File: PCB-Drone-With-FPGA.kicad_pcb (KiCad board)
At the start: 4 copper layers, 100 x 100 mm, 45 parts, among them J501 SMA-RP, U1 10CL040_F484, U401 ICM-20948, U402 BNO055, U403 DPS422XTSA1, U404 MCP3208, U405 TXB0104PWR, U501 nRF24L01P, U502 RFX2401C, X501 16MHz

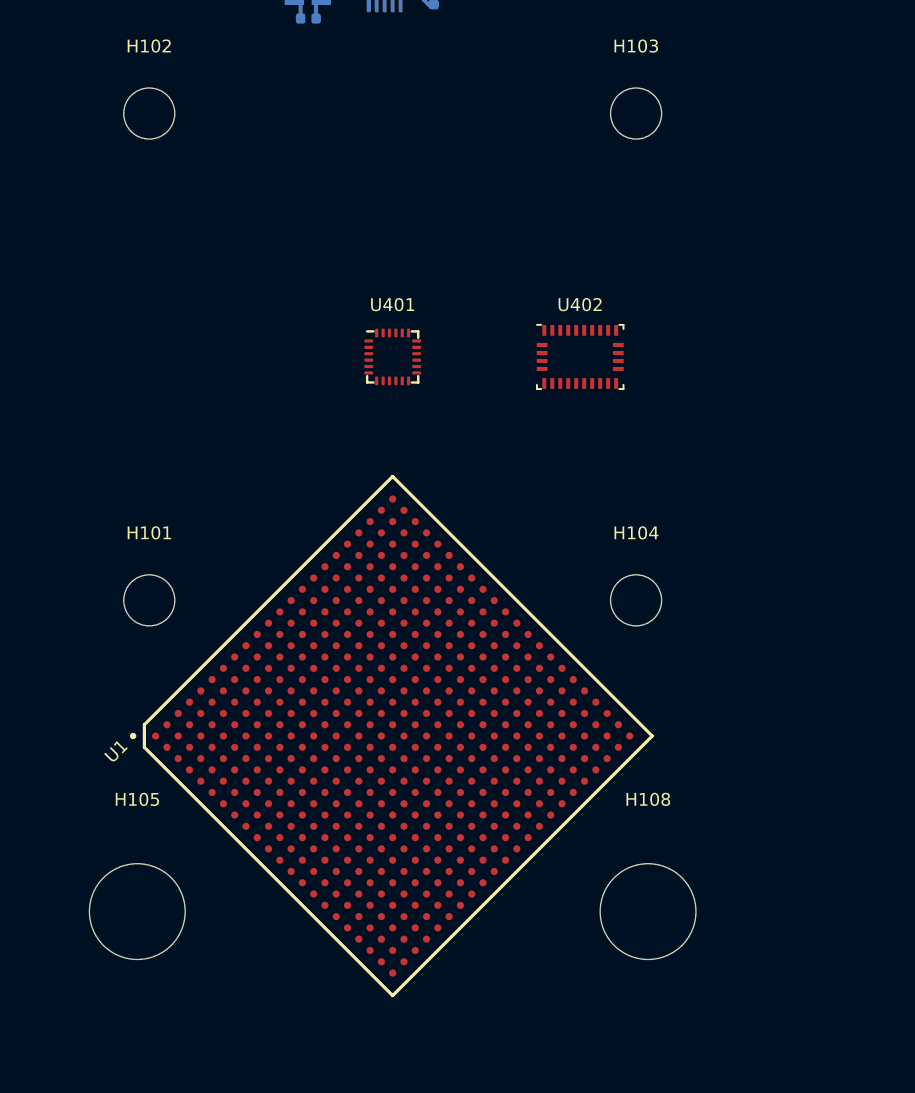
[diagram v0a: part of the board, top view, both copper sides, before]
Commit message: Continued work on schematic and board planning
Signed-off-by: Eldalote <Eldalote.Electronics@gmail.com>
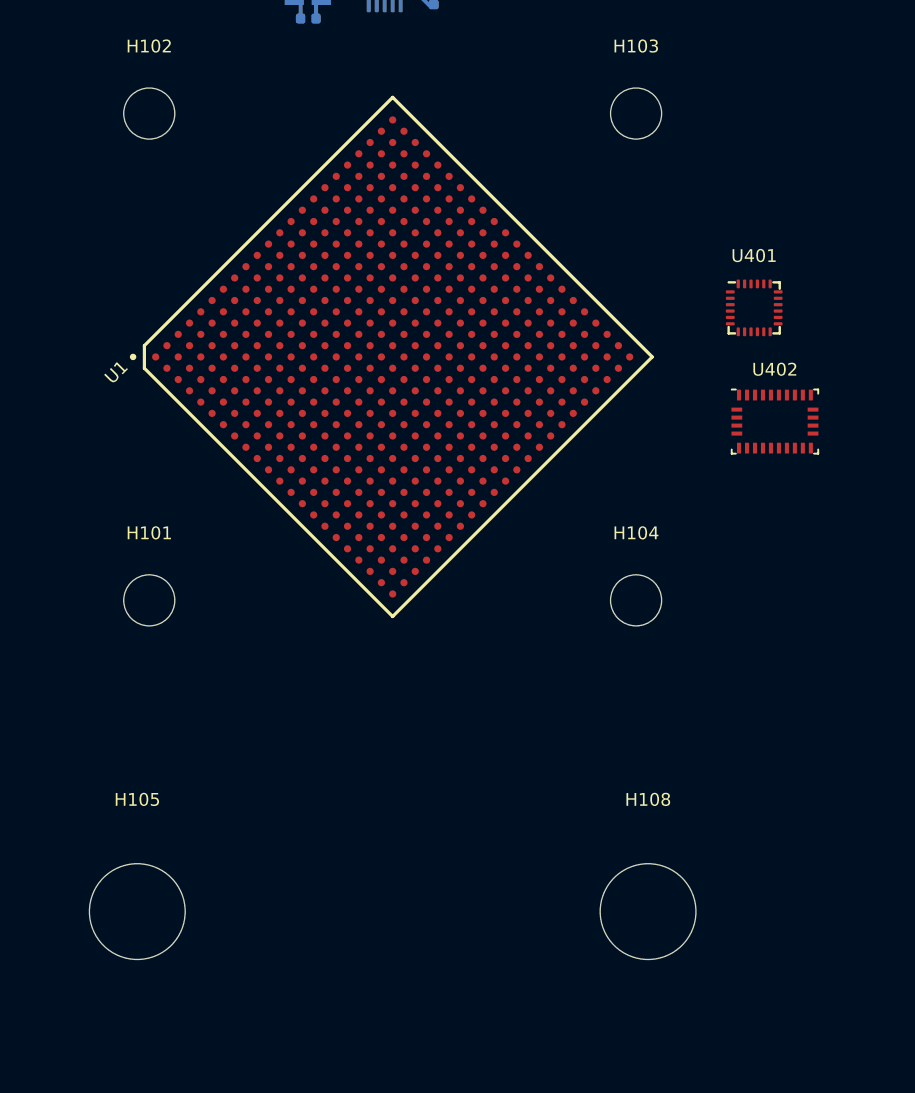
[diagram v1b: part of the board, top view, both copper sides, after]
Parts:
- moved U1 23.8 mm to (150.2, 100.2)
- moved U401 22.9 mm to (172.9, 97.2)
- moved U402 12.9 mm to (174.2, 104.3)

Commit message: More of the same
Signed-off-by: Eldalote <Eldalote.Electronics@gmail.com>
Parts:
- removed H107, H108: MountingHole, MountingHole:MountingHole_6mm
- added J201: PJ-102A, digikey-footprints:Barrel_Jack_5.5mmODx2.1mmID_PJ-102A, F.Cu at (152.5, 134.9)
- added J601: Conn_02x10_Row_Letter_First, Connector_PinHeader_2.54mm:PinHeader_2x10_P2.54mm_Vertical, F.Cu at (114.0, 42.7)
- added J602: Conn_02x10_Row_Letter_First, Connector_PinHeader_2.54mm:PinHeader_2x10_P2.54mm_Vertical, F.Cu at (144.0, 42.9)
- added JP201: Jumper_NC_Dual, Connector_PinHeader_2.54mm:PinHeader_1x03_P2.54mm_Vertical, F.Cu at (179.5, 122.1)
- added U201: TPS54331DR, SamacSys_Parts:SOIC127P600X175-8N, F.Cu at (112.7, 117.7)
- added U202: TPS54331DR, SamacSys_Parts:SOIC127P600X175-8N, F.Cu at (146.4, 108.9)
- added U203: TPS54331DR, SamacSys_Parts:SOIC127P600X175-8N, F.Cu at (153.5, 87.7)
- added U204: TPS73701DCQ, SamacSys_Parts:SOT127P706X180-6N, F.Cu at (106.3, 86.7)
- added U301: FT232H, Package_QFP:LQFP-48_7x7mm_P0.5mm, F.Cu at (130.3, 122.5)
- added U406: TXB0108PWR, digikey-footprints:TSSOP-20_W4.4mm, F.Cu at (120.9, 101.6)
- C501, C502, C503, C504, C505, C506, C507, C508, C509, C510, C511, C512, C513, C514, C515, C516, C517, J501, L501, L502, L503, L504, L505, R501, R502, R503, R504, U501, U502, X501: moved to F.Cu
- U1: moved to B.Cu
- U405: value TXB0104PWR -> TXB0108PWR; footprint digikey-footprints:TSSOP-14_W4.4mm -> digikey-footprints:TSSOP-20_W4.4mm
- moved U404 122.1 mm to (112.4, 107.5)
- moved U405 104.9 mm to (120.8, 109.0), turned to 90 degrees
- moved U403 98.3 mm to (138.2, 115.8)
- moved H105 63.3 mm to (114.8, 74.8)
- moved U401 44.8 mm to (130.0, 110.0)
- moved U402 37.0 mm to (137.6, 109.7)
- moved C512 29.7 mm to (126.1, 56.1)
- moved C503 29.2 mm to (126.4, 65.8)
- moved R501 28.3 mm to (126.9, 63.8), turned to 180 degrees
- moved C511 27.9 mm to (127.1, 55.1)
- moved C510 27.9 mm to (127.1, 57.1)
- moved C502 27.4 mm to (127.4, 65.8)
- moved C501 27.4 mm to (127.4, 67.7)
- moved U1 24.2 mm to (130.0, 87.0), turned to 315 degrees
- moved C513 24.1 mm to (129.1, 53.0), turned to 0 degrees
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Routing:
- net GND: track 18.1 -> 14.1 mm, vias 2 -> 0
- added copper zone on F.Cu, net GND
- removed copper zone on B.Cu, net GND
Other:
- board size 100 x 100 mm -> 60 x 100 mm

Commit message: Further work
Signed-off-by: Eldalote <Eldalote.Electronics@gmail.com>
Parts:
- removed J601, J602: Conn_02x10_Row_Letter_First, Connector_PinHeader_2.54mm:PinHeader_2x10_P2.54mm_Vertical
- added C201: 22uF 25v, Capacitor_SMD:C_0805_2012Metric, F.Cu at (86.5, 133.6)
- added C202: 10pF, Capacitor_SMD:C_0402_1005Metric, F.Cu at (80.1, 142.7)
- added C203: 1nF, Capacitor_SMD:C_0402_1005Metric, F.Cu at (85.8, 138.6)
- added C204: 8n2F, Capacitor_SMD:C_0603_1608Metric, F.Cu at (76.6, 142.9)
- added C205: 100nF, Capacitor_SMD:C_0402_1005Metric, F.Cu at (83.0, 142.7)
- added C206: 47uF, Resistor_SMD:R_1206_3216Metric, F.Cu at (66.2, 141.5)
- added C207: 47uF, Resistor_SMD:R_1206_3216Metric, F.Cu at (71.8, 143.3)
- added C208: 47uF, Resistor_SMD:R_1206_3216Metric, F.Cu at (66.2, 144.8)
- added D201: 3A 60v, Diode_SMD:D_SMC, F.Cu at (68.8, 136.0)
- added J301: UJ2-MBH-1-SMT-TR, digikey-footprints:USB_Mini_B_Female_UJ2-MBH-1-SMT-TR, F.Cu at (130.7, 139.7)
- added J701: Conn_02x10, Connector_PinHeader_2.54mm:PinHeader_2x10_P2.54mm_Vertical, F.Cu at (113.7, 42.9)
- added J702: Conn_02x07, Connector_PinHeader_2.54mm:PinHeader_2x07_P2.54mm_Vertical, F.Cu at (102.6, 103.1)
- added J703: Conn_02x10, Connector_PinHeader_2.54mm:PinHeader_2x10_P2.54mm_Vertical, F.Cu at (143.9, 43.2)
- added J704: Conn_02x04, Connector_PinHeader_2.54mm:PinHeader_2x04_P2.54mm_Vertical, F.Cu at (154.3, 116.8)
- added J705: Conn_02x05, Connector_PinHeader_2.54mm:PinHeader_2x05_P2.54mm_Vertical, F.Cu at (154.4, 93.8)
- added L201: 5u6H, Inductor_SMD:L_Bourns_SRN8040TA, F.Cu at (79.3, 136.9)
- added R201: 330K, Resistor_SMD:R_0402_1005Metric, F.Cu at (80.1, 144.7)
- added R202: 68K, Resistor_SMD:R_0402_1005Metric, F.Cu at (85.8, 140.6)
- added R203: 62K, Resistor_SMD:R_0603_1608Metric, F.Cu at (86.3, 136.3)
- added R204: 10K, Resistor_SMD:R_0402_1005Metric, F.Cu at (83.0, 144.7)
- added R205: 1.8K, Resistor_SMD:R_0603_1608Metric, F.Cu at (76.6, 145.4)
- added R206: 100R, Resistor_SMD:R_0402_1005Metric, F.Cu at (85.9, 142.6)
- moved JP201 75.4 mm to (104.2, 125.6)
- moved LOGO101 46.0 mm to (158.8, 73.8)
- moved U405 27.6 mm to (147.5, 116.0)
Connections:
- U201 pad 7: Net-(U201-Pad7) -> GND
- U202 pad 2: +10V -> Net-(U202-Pad2)
- U203 pad 2: +10V -> Net-(U203-Pad2)

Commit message: Made progress woth power
Signed-off-by: Jan Mart Liewes <Eldalote.Electronics@gmail.com>
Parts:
- removed C201: 22uF 25v, Capacitor_SMD:C_0805_2012Metric
- removed C202: 10pF, Capacitor_SMD:C_0402_1005Metric
- removed C203: 1nF, Capacitor_SMD:C_0402_1005Metric
- removed C204: 8n2F, Capacitor_SMD:C_0603_1608Metric
- removed C205: 100nF, Capacitor_SMD:C_0402_1005Metric
- removed C206, C207, C208: 47uF, Resistor_SMD:R_1206_3216Metric
- removed C505: 22pF, Capacitor_SMD:C_0402_1005Metric
- removed D201: 3A 60v, Diode_SMD:D_SMC
- removed L201: 5u6H, Inductor_SMD:L_Bourns_SRN8040TA
- removed R201: 330K, Resistor_SMD:R_0402_1005Metric
- removed R202: 68K, Resistor_SMD:R_0402_1005Metric
- removed R203: 62K, Resistor_SMD:R_0603_1608Metric
- removed R204: 10K, Resistor_SMD:R_0402_1005Metric
- removed R205: 1.8K, Resistor_SMD:R_0603_1608Metric
- removed R206: 100R, Resistor_SMD:R_0402_1005Metric
- removed U201, U202, U203: TPS54331DR, SamacSys_Parts:SOIC127P600X175-8N
- removed U204: TPS73701DCQ, SamacSys_Parts:SOT127P706X180-6N
- removed U405: TXB0108PWR, digikey-footprints:TSSOP-20_W4.4mm
- added C301: 10uF 25v, Capacitor_SMD:C_0805_2012Metric, F.Cu at (166.4, 56.2)
- added C302: 100nF 16v, Capacitor_SMD:C_0402_1005Metric, F.Cu at (170.1, 56.7)
- added C303: 22uF 25v, Capacitor_SMD:C_0805_2012Metric, F.Cu at (172.9, 54.2)
- added C304: 22uF 25v, Capacitor_SMD:C_0805_2012Metric, F.Cu at (178.1, 49.7)
- added C401: 10uF, Capacitor_SMD:C_0805_2012Metric, F.Cu at (191.6, 79.7)
- added C402: 1uF, Capacitor_SMD:C_0603_1608Metric, F.Cu at (196.1, 77.7)
- added C403: 1uF, Capacitor_SMD:C_0603_1608Metric, F.Cu at (195.8, 80.2)
- added C404: 22uF, Capacitor_SMD:C_0805_2012Metric, F.Cu at (196.2, 75.0)
- added C805: 15pF, Capacitor_SMD:C_0402_1005Metric, F.Cu at (135.2, 63.8)
- added L301: 4.7uH 2.6ADC, Eldalote-footprints:L_5030_TAIYO_YUDEN, F.Cu at (167.5, 51.5)
- added L401: 1uH, Eldalote-footprints:L_3012_TDK, F.Cu at (191.8, 75.7)
- added U301: AP63205WU-7, SamacSys_Parts:SOT95P280X100-6N, F.Cu at (173.3, 50.5)
- added U402: NCP115ASN250T2G, SamacSys_Parts:SOT95P275X110-5N, F.Cu at (186.9, 75.8)
- added U501: AP63200WU-7, SamacSys_Parts:SOT95P280X100-6N, F.Cu at (207.2, 75.8)
- C804: renamed from C504; value 22pF -> 15pF
- U401: value ICM-20948 -> SC189ZSKTRT; footprint Sensor_Motion:InvenSense_QFN-24_3x3mm_P0.4mm -> SamacSys_Parts:SOT95P280X145-5N
- moved U401 64.0 mm to (186.8, 80.5)
- renumbered C501 to C801, C502 to C802, C503 to C803, C506 to C806, C507 to C807, C508 to C808, C509 to C809, C510 to C810, C511 to C811, C512 to C812, C513 to C813, C514 to C814, C515 to C815, C516 to C816, C517 to C817, J701 to J1001, J702 to J1002, J703 to J1003, J704 to J1004, J705 to J1005, J301 to J601, J501 to J801, L501 to L801, L502 to L802, L503 to L803, L504 to L804, L505 to L805, R501 to R801, R502 to R802, R503 to R803, R504 to R804, U1 to U1201, U301 to U601, U402 to U701, U403 to U702, U404 to U703, U406 to U704, U501 to U801, U502 to U802, X501 to X801
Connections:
- U401 pad 1: Net-(U401-Pad1) -> +5V
- U401 pad 2: Net-(U401-Pad2) -> GND
- U401 pad 3: Net-(U401-Pad3) -> +5V
- U401 pad 4: Net-(U401-Pad4) -> +3V3

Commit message: Finished v0.1 of power, and v0.1 of sensors.
Signed-off-by: Jan Mart Liewes <Eldalote.Electronics@gmail.com>
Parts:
- added C501: 10uF, Capacitor_SMD:C_0805_2012Metric, F.Cu at (195.7, 97.6)
- added C502: 100nF, Capacitor_SMD:C_0402_1005Metric, F.Cu at (195.0, 100.1)
- added C503: 100pF, Capacitor_SMD:C_0402_1005Metric, F.Cu at (198.4, 103.0)
- added C504: 22uF, Capacitor_SMD:C_0805_2012Metric, F.Cu at (194.8, 103.3)
- added C505: 22uF, Capacitor_SMD:C_0805_2012Metric, F.Cu at (200.2, 97.6)
- added C701: 100nF, Capacitor_SMD:C_0402_1005Metric, F.Cu at (78.1, 100.1)
- added C702: 2u2F, Capacitor_SMD:C_0603_1608Metric, F.Cu at (74.6, 100.4)
- added C703: 100nF, Capacitor_SMD:C_0402_1005Metric, F.Cu at (78.8, 107.6)
- added C704: 10nF, Capacitor_SMD:C_0402_1005Metric, F.Cu at (74.1, 109.6)
- added C705: 100nF, Capacitor_SMD:C_0402_1005Metric, F.Cu at (75.9, 107.6)
- added C706: 100nF, Capacitor_SMD:C_0805_2012Metric_Pad1.15x1.40mm_HandSolder, F.Cu at (65.5, 100.6)
- added C707: 100nF, Capacitor_SMD:C_0805_2012Metric_Pad1.15x1.40mm_HandSolder, F.Cu at (60.4, 106.9)
- added C708: 100nF, Capacitor_SMD:C_0402_1005Metric, F.Cu at (73.6, 105.6)
- added C709: 100nF, Capacitor_SMD:C_0402_1005Metric, F.Cu at (78.1, 102.1)
- added C710: 4n7F, Capacitor_SMD:C_0603_1608Metric, F.Cu at (64.8, 109.6)
- added C711: 22pF, Capacitor_SMD:C_0603_1608Metric, F.Cu at (69.6, 107.9)
- added C712: 22pF, Capacitor_SMD:C_0603_1608Metric, F.Cu at (74.1, 103.3)
- added C713: 100nF, Capacitor_SMD:C_0402_1005Metric, F.Cu at (77.0, 109.6)
- added C714: 1uF, Capacitor_SMD:C_0805_2012Metric_Pad1.15x1.40mm_HandSolder, F.Cu at (65.2, 106.9)
- added C715: 100nF, Capacitor_SMD:C_0805_2012Metric_Pad1.15x1.40mm_HandSolder, F.Cu at (60.4, 109.9)
- added C716: 100nF, Capacitor_SMD:C_0402_1005Metric, F.Cu at (68.3, 110.1)
- added C717: 1uF, Capacitor_SMD:C_0805_2012Metric_Pad1.15x1.40mm_HandSolder, F.Cu at (70.2, 100.6)
- added C718: 100nF, Capacitor_SMD:C_0805_2012Metric_Pad1.15x1.40mm_HandSolder, F.Cu at (65.2, 104.0)
- added L501: 2u2H, Eldalote-footprints:L_4018_Bourns, F.Cu at (190.7, 99.0)
- added R501: 30k9, Resistor_SMD:R_0805_2012Metric_Pad1.15x1.40mm_HandSolder, F.Cu at (190.2, 103.3)
- added R502: 62k, Resistor_SMD:R_0805_2012Metric, F.Cu at (199.2, 100.5)
- added R701: 4k7, Resistor_SMD:R_0402_1005Metric, F.Cu at (73.0, 107.6)
- added R702: 4k7, Resistor_SMD:R_0402_1005Metric, F.Cu at (71.2, 110.1)
- added R703: 10k, Resistor_SMD:R_0402_1005Metric, F.Cu at (76.5, 105.6)
- added R704: 10K, Resistor_SMD:R_0805_2012Metric_Pad1.15x1.40mm_HandSolder, F.Cu at (60.4, 104.0)
- added U701: ICM-20602, Package_LGA:LGA-16_3x3mm_P0.5mm_LayoutBorder3x5y, F.Cu at (69.8, 104.4)
- added Y701: 32.7KHz, Crystal:Crystal_SMD_3215-2Pin_3.2x1.5mm, F.Cu at (60.6, 100.8)
- L301: value 4.7uH 2.6ADC -> 4u7H 2.6ADC
- moved U501 33.6 mm to (185.1, 101.2)
- renumbered U704 to U702, U701 to U703, U702 to U704, U703 to U705
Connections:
- net Net-(U701-Pad14) renamed BNO_INT
- net Net-(U702-Pad2) renamed DPS_CSn
- net Net-(U702-Pad3) renamed DPS_MOSI
- net Net-(U702-Pad4) renamed DPS_SCLK
- net Net-(U702-Pad5) renamed DPS_MISO
- net Net-(U703-Pad2) renamed ADC_CH1
- net Net-(U703-Pad3) renamed ADC_CH2
- net Net-(U703-Pad4) renamed ADC_CH3
- net Net-(U703-Pad5) renamed ADC_CH4
- net Net-(U703-Pad6) renamed ADC_CH5
- net Net-(U704-Pad1) renamed ADC_CSn
- net Net-(U704-Pad12) renamed /Sensors/5v_GPIO_5v_3
- net Net-(U704-Pad13) renamed /Sensors/5v_GPIO_5v_2
- net Net-(U704-Pad14) renamed /Sensors/5v_GPIO_5v_1
- net Net-(U704-Pad15) renamed /Sensors/5v_GPIO_5v_0
- net Net-(U704-Pad3) renamed ADC_MOSI
- net Net-(U704-Pad4) renamed ADC_MISO
- net Net-(U704-Pad5) renamed ADC_SCLK
- net Net-(U704-Pad6) renamed 5v_GPIO_0
- net Net-(U704-Pad7) renamed 5v_GPIO_1
- net Net-(U704-Pad8) renamed 5v_GPIO_2
- net Net-(U704-Pad9) renamed 5v_GPIO_3
- U501 pad 2: Net-(U501-Pad2) -> +5V
- U501 pad 3: Net-(U501-Pad3) -> +5V
- U501 pad 4: Net-(U501-Pad4) -> GND
- U702 pad 11: Net-(U704-Pad11) -> GND
- U702 pad 16: Net-(U704-Pad16) -> /Sensors/5v_ADC_CLK
- U702 pad 17: Net-(U704-Pad17) -> /Sensors/5v_ADC_Dout
- U702 pad 18: Net-(U704-Pad18) -> /Sensors/5v_ADC_Din
- U702 pad 19: Net-(U704-Pad19) -> +5V
- U702 pad 2: Net-(U704-Pad2) -> +3V3
- U702 pad 20: Net-(U704-Pad20) -> /Sensors/5v_ADC_CSn
- U703 pad 11: Net-(U701-Pad11) -> BNO_NRESET
- U703 pad 15: Net-(U701-Pad15) -> GND
- U703 pad 16: Net-(U701-Pad15) -> GND
- U703 pad 17: Net-(U701-Pad17) -> GND
- U703 pad 18: Net-(U701-Pad18) -> GND
- U703 pad 19: Net-(U701-Pad19) -> BNO_SCL
- U703 pad 2: Net-(U701-Pad2) -> GND
- U703 pad 20: Net-(U701-Pad20) -> BNO_SDA
- U703 pad 25: Net-(U701-Pad15) -> GND
- U703 pad 28: Net-(U701-Pad28) -> +3V3
- U703 pad 3: Net-(U701-Pad3) -> +3V3
- U703 pad 4: Net-(U701-Pad4) -> +3V3
- U703 pad 5: Net-(U701-Pad5) -> GND
- U703 pad 6: Net-(U701-Pad6) -> GND
- U704 pad 1: Net-(U702-Pad1) -> GND
- U704 pad 6: Net-(U702-Pad6) -> +3V3
- U704 pad 7: Net-(U702-Pad7) -> GND
- U704 pad 8: Net-(U702-Pad8) -> +3V3
- U705 pad 1: Net-(U703-Pad1) (its old number) -> ADC_CH0
- U705 pad 10: Net-(U703-Pad10) (its old number) -> /Sensors/5v_ADC_CSn
- U705 pad 11: Net-(U703-Pad11) -> /Sensors/5v_ADC_Din
- U705 pad 12: Net-(U703-Pad12) (its old number) -> /Sensors/5v_ADC_Dout
- U705 pad 13: Net-(U703-Pad13) (its old number) -> /Sensors/5v_ADC_CLK
- U705 pad 14: Net-(U703-Pad14) -> GNDA
- U705 pad 15: Net-(U703-Pad15) -> +5V
- U705 pad 16: Net-(U703-Pad16) -> +5V
- U705 pad 7: Net-(U703-Pad7) (its old number) -> ADC_CH6
- U705 pad 8: Net-(U703-Pad8) (its old number) -> ADC_CH7
- U705 pad 9: Net-(U703-Pad9) -> GND
